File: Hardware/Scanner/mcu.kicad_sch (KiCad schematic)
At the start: 8 parts, among them Q1 BSS138DW-7-F, U6 AS7341-DLGT

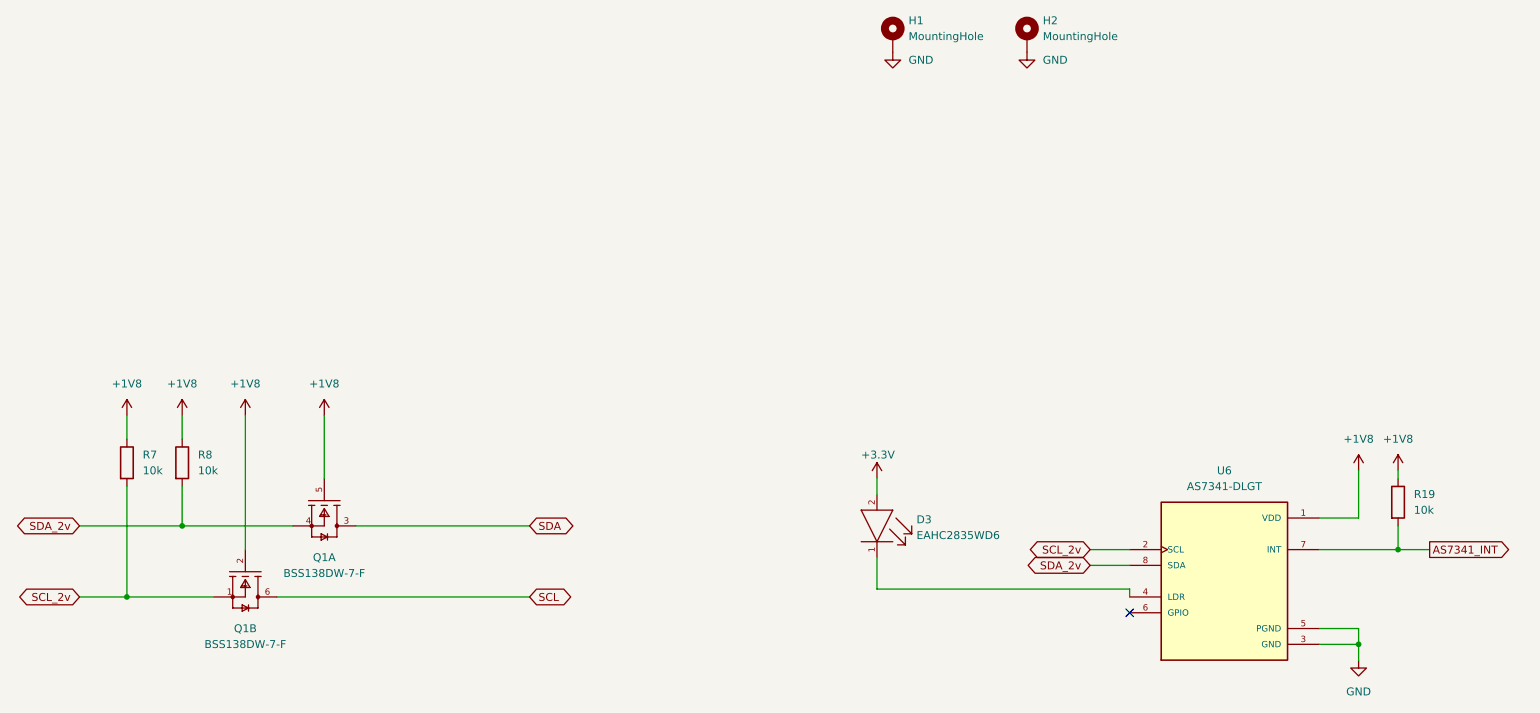
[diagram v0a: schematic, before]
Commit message: added footprint for MTSM2601SMF1-100
Signed-off-by: lokimetasmith <lokimail@gmail.com>
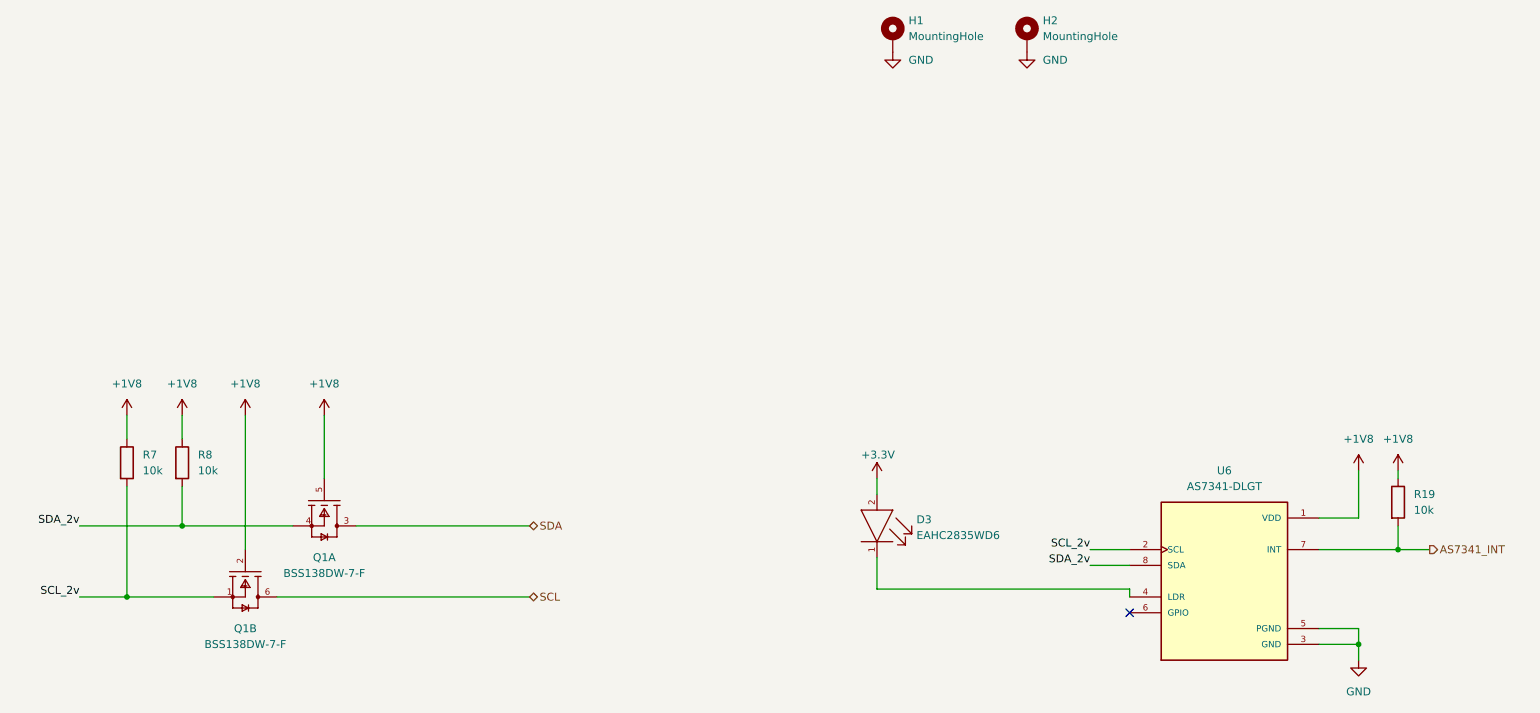
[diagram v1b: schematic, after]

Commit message: lots of changes, added footprints, fixed broken schemaitcs, fixed kicad 7.0 issues
Signed-off-by: lokimetasmith <lokimail@gmail.com>
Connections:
- net +3V3 renamed +3.3V

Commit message: updated schematic, and layout, updated bom, fully converted to 3.3v for Voltage input only
Signed-off-by: lokimetasmith <lokimail@gmail.com>
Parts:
- D3: automotive No -> (none); category Diode -> (none); colour White -> (none); device class L1 Optoelectronics -> (none); device class L2 LEDs -> (none); device class L3 unset -> (none); forward current 150mA -> (none); forward voltage 3.4V -> (none); height 0.85mm -> (none); lead free Yes -> (none); led orientation Top View -> (none); library id 70d3c750636d3268 -> (none); max junction temp +115°C -> (none); package PLCC2 -> (none); power dissipation 630mW -> (none); reverse voltage 5V -> (none); rohs Yes -> (none); temperature range high +85°C -> (none); temperature range low -40°C -> (none); viewing angle 120° -> (none)
- R19, R7, R8: digikey description (none) -> RES 10K OHM 5% 1/10W 0603; digikey part number (none) -> 311-10KGRCT-ND; mouser description (none) -> CRGH0603J10K; mouser part number (none) -> 279-CRGH0603J10K
- U6: digikey description (none) -> SENSOR OPT AMBIENT 8OLGA; digikey part number (none) -> AS7341-DLGTCT-ND
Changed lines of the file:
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@@
+      (effects (font (size 1.27 1.27)) hide)
+    )
+    (property "mouser description" "CRGH0603J10K" (at 68.58 100.33 0)
+      (effects (font (size 1.27 1.27)) hide)
+    )
+    (property "mouser part number" "279-CRGH0603J10K" (at 68.58 100.33 0)
+      (effects (font (size 1.27 1.27)) hide)
+    )
+    (property "digikey description" "RES 10K OHM 5% 1/10W 0603" (at 68.58 100.33 0)
+      (effects (font (size 1.27 1.27)) hide)
+    )
+    (property "digikey part number" "311-10KGRCT-ND" (at 68.58 100.33 0)
       (effects (font (size 1.27 1.27)) hide)
     )
@@
       (effects (font (size 1.27 1.27)) (justify left) hide)
     )
-    (property "automotive" "No" (at 200.66 102.87 0)
-      (effects (font (size 1.27 1.27)) (justify left) hide)
-    )
-    (property "category" "Diode" (at 203.2 102.87 0)
-      (effects (font (size 1.27 1.27)) (justify left) hide)
-    )
-    (property "colour" "White" (at 205.74 102.87 0)
-      (effects (font (size 1.27 1.27)) (justify left) hide)
-    )
-    (property "device class L1" "Optoelectronics" (at 208.28 102.87 0)
-      (effects (font (size 1.27 1.27)) (justify left) hide)
-    )
-    (property "device class L2" "LEDs" (at 210.82 102.87 0)
-      (effects (font (size 1.27 1.27)) (justify left) hide)
-    )
-    (property "device class L3" "unset" (at 213.36 102.87 0)
-      (effects (font (size 1.27 1.27)) (justify left) hide)
-    )
     (property "digikey description" "LED COOL WHITE 6500K 2SMD" (at 215.9 102.87 0)
       (effects (font (size 1.27 1.27)) (justify left) hide)
@@
       (effects (font (size 1.27 1.27)) (justify left) hide)
     )
-    (property "forward current" "150mA" (at 220.98 102.87 0)
-      (effects (font (size 1.27 1.27)) (justify left) hide)
-    )
-    (property "forward voltage" "3.4V" (at 223.52 102.87 0)
-      (effects (font (size 1.27 1.27)) (justify left) hide)
-    )
-    (property "height" "0.85mm" (at 226.06 102.87 0)
-      (effects (font (size 1.27 1.27)) (justify left) hide)
-    )
-    (property "lead free" "Yes" (at 228.6 102.87 0)
-      (effects (font (size 1.27 1.27)) (justify left) hide)
-    )
-    (property "led orientation" "Top View" (at 231.14 102.87 0)
-      (effects (font (size 1.27 1.27)) (justify left) hide)
-    )
-    (property "library id" "70d3c750636d3268" (at 233.68 102.87 0)
-      (effects (font (size 1.27 1.27)) (justify left) hide)
-    )
     (property "manufacturer" "Everlight" (at 236.22 102.87 0)
       (effects (font (size 1.27 1.27)) (justify left) hide)
     )
-    (property "max junction temp" "+115°C" (at 238.76 102.87 0)
-      (effects (font (size 1.27 1.27)) (justify left) hide)
-    )
     (property "mouser description" "White High Power Lighting LED" (at 241.3 102.87 0)
       (effects (font (size 1.27 1.27)) (justify left) hide)
     )
     (property "mouser part number" "638-EAHC2835WD6" (at 243.84 102.87 0)
-      (effects (font (size 1.27 1.27)) (justify left) hide)
-    )
-    (property "package" "PLCC2" (at 246.38 102.87 0)
-      (effects (font (size 1.27 1.27)) (justify left) hide)
-    )
-    (property "power dissipation" "630mW" (at 248.92 102.87 0)
-      (effects (font (size 1.27 1.27)) (justify left) hide)
-    )
-    (property "reverse voltage" "5V" (at 251.46 102.87 0)
-      (effects (font (size 1.27 1.27)) (justify left) hide)
-    )
-    (property "rohs" "Yes" (at 254 102.87 0)
-      (effects (font (size 1.27 1.27)) (justify left) hide)
-    )
-    (property "temperature range high" "+85°C" (at 256.54 102.87 0)
-      (effects (font (size 1.27 1.27)) (justify left) hide)
-    )
-    (property "temperature range low" "-40°C" (at 259.08 102.87 0)
-      (effects (font (size 1.27 1.27)) (justify left) hide)
-    )
-    (property "viewing angle" "120°" (at 261.62 102.87 0)
       (effects (font (size 1.27 1.27)) (justify left) hide)
     )
@@
           (reference "Q1") (unit 1)
         )
+        (path "/a818e058-3544-4da8-96fb-1a428660711f/a8dcb7a4-48cf-403e-b881-d44234291c62"
+          (reference "Q1") (unit 1)
+        )
       )
     )
@@
       (effects (font (size 1.27 1.27)) hide)
     )
+    (property "mouser description" "CRGH0603J10K" (at 264.16 106.68 0)
+      (effects (font (size 1.27 1.27)) hide)
+    )
+    (property "mouser part number" "279-CRGH0603J10K" (at 264.16 106.68 0)
+      (effects (font (size 1.27 1.27)) hide)
+    )
+    (property "digikey description" "RES 10K OHM 5% 1/10W 0603" (at 264.16 106.68 0)
+      (effects (font (size 1.27 1.27)) hide)
+    )
+    (property "digikey part number" "311-10KGRCT-ND" (at 264.16 106.68 0)
+      (effects (font (size 1.27 1.27)) hide)
+    )
     (pin "1")
     (pin "2")
@@
       (effects (font (size 1.27 1.27)) hide)
     )
+    (property "mouser description" "CRGH0603J10K" (at 59.69 100.33 0)
+      (effects (font (size 1.27 1.27)) hide)
+    )
+    (property "mouser part number" "279-CRGH0603J10K" (at 59.69 100.33 0)
+      (effects (font (size 1.27 1.27)) hide)
+    )
+    (property "digikey description" "RES 10K OHM 5% 1/10W 0603" (at 59.69 100.33 0)
+      (effects (font (size 1.27 1.27)) hide)
+    )
+    (property "digikey part number" "311-10KGRCT-ND" (at 59.69 100.33 0)
+      (effects (font (size 1.27 1.27)) hide)
+    )
     (pin "1")
     (pin "2")
@@
       (effects (font (size 1.27 1.27)) (justify left bottom) hide)
     )
-    (pin "1")
+    (property "digikey description" "SENSOR OPT AMBIENT 8OLGA" (at 236.22 119.38 0)
+      (effects (font (size 1.27 1.27)) hide)
+    )
+    (property "digikey part number" "AS7341-DLGTCT-ND" (at 236.22 119.38 0)
+      (effects (font (size 1.27 1.27)) hide)
+    )
+    (pin "1")

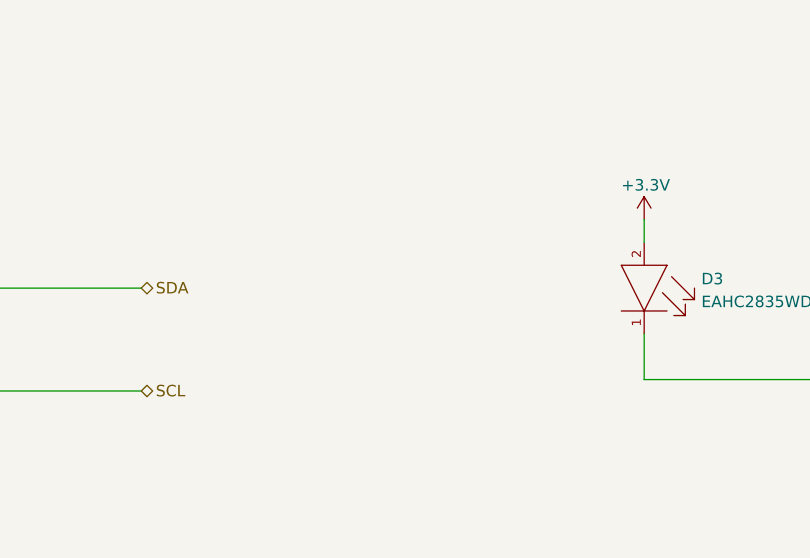
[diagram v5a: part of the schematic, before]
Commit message: added decoupling capactitors, added footprint for 3d model, need to verify new footprint
Signed-off-by: lokimetasmith <lokimail@gmail.com>
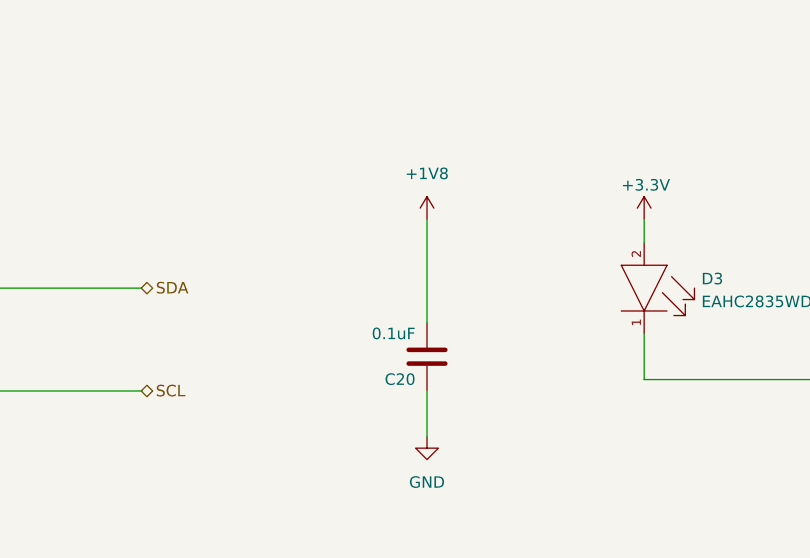
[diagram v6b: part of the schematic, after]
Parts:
- added C20: 0.1uF, Capacitor_SMD:C_0603_1608Metric_Pad1.08x0.95mm_HandSolder, symbol Device:C
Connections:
- net +1V8: now also C20.2
- net GND: now also C20.1
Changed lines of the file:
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@@
+    (stroke (width 0) (type default))
+  )
+  (wire (pts (xy 156.21 102.87) (xy 156.21 114.3))
     (stroke (width 0) (type default))
   )
@@
   )
   (wire (pts (xy 52.07 121.92) (xy 59.69 121.92))
+    (stroke (width 0) (type default))
+  )
+  (wire (pts (xy 156.21 121.92) (xy 156.21 127))
     (stroke (width 0) (type default))
   )
@@
         (path "/a818e058-3544-4da8-96fb-1a428660711f/f3879066-a91b-415e-b241-18f9d05de4a2"
           (reference "#PWR0112") (unit 1)
+        )
+      )
+    )
+  )
+  (symbol (lib_id "power:GND") (at 156.21 127 0) (unit 1)
+    (in_bom yes) (on_board yes) (dnp no) (fields_autoplaced)
+    (property "Reference" "#PWR0125" (at 156.21 133.35 0)
+      (effects (font (size 1.27 1.27)) hide)
+    )
+    (property "Value" "GND" (at 156.21 132.08 0)
+      (effects (font (size 1.27 1.27)))
+    )
+    (property "Footprint" "" (at 156.21 127 0)
+      (effects (font (size 1.27 1.27)) hide)
+    )
+    (property "Datasheet" "" (at 156.21 127 0)
+      (effects (font (size 1.27 1.27)) hide)
+    )
+    (pin "1")
+    (instances
+      (project "RoundScanner"
+        (path "/a818e058-3544-4da8-96fb-1a428660711f/5869e7b3-0d61-455b-97ad-e4e8b4829f27"
+          (reference "#PWR0125") (unit 1)
+        )
+        (path "/a818e058-3544-4da8-96fb-1a428660711f/f3879066-a91b-415e-b241-18f9d05de4a2"
+          (reference "#PWR046") (unit 1)
         )
       )
@@
         (path "/a818e058-3544-4da8-96fb-1a428660711f/f3879066-a91b-415e-b241-18f9d05de4a2"
           (reference "#PWR0109") (unit 1)
+        )
+      )
+    )
+  )
+  (symbol (lib_id "power:+1V8") (at 156.21 102.87 0) (unit 1)
+    (in_bom yes) (on_board yes) (dnp no) (fields_autoplaced)
+    (property "Reference" "#PWR0130" (at 156.21 106.68 0)
+      (effects (font (size 1.27 1.27)) hide)
+    )
+    (property "Value" "+1V8" (at 156.21 97.79 0)
+      (effects (font (size 1.27 1.27)))
+    )
+    (property "Footprint" "" (at 156.21 102.87 0)
+      (effects (font (size 1.27 1.27)) hide)
+    )
+    (property "Datasheet" "" (at 156.21 102.87 0)
+      (effects (font (size 1.27 1.27)) hide)
+    )
+    (pin "1")
+    (instances
+      (project "RoundScanner"
+        (path "/a818e058-3544-4da8-96fb-1a428660711f/5869e7b3-0d61-455b-97ad-e4e8b4829f27"
+          (reference "#PWR0130") (unit 1)
+        )
+        (path "/a818e058-3544-4da8-96fb-1a428660711f/f3879066-a91b-415e-b241-18f9d05de4a2"
+          (reference "#PWR045") (unit 1)
         )
       )
@@
         )
       )
+    )
+  )
+  (symbol (lib_id "Device:C") (at 156.21 118.11 180) (unit 1)
+    (in_bom yes) (on_board yes) (dnp no)
+    (property "Reference" "C20" (at 154.94 120.65 0)
+      (effects (font (size 1.27 1.27)) (justify left))
+    )
+    (property "Value" "0.1uF" (at 154.94 115.57 0)
+      (effects (font (size 1.27 1.27)) (justify left))
+    )
+    (property "Footprint" "Capacitor_SMD:C_0603_1608Metric_Pad1.08x0.95mm_HandSolder" (at 155.2448 114.3 0)
+      (effects (font (size 1.27 1.27)) hide)
+    )
+    (property "Datasheet" "~" (at 156.21 118.11 0)
+      (effects (font (size 1.27 1.27)) hide)
+    )
+    (property "digikey description" "CAP CER 0.1UF 16V X7R 0603" (at 156.21 118.11 0)
+      (effects (font (size 1.27 1.27)) hide)
+    )
+    (property "digikey part number" "311-1088-1-ND" (at 156.21 118.11 0)
+      (effects (font (size 1.27 1.27)) hide)
+    )
+    (pin "1")
+    (pin "2")
+    (instances
+      (project "RoundScanner"
+        (path "/a818e058-3544-4da8-96fb-1a428660711f/5869e7b3-0d61-455b-97ad-e4e8b4829f27"
+          (reference "C20") (unit 1)
+        )
+        (path "/a818e058-3544-4da8-96fb-1a428660711f/f3879066-a91b-415e-b241-18f9d05de4a2"
+          (reference "C20") (unit 1)
+        )
+      )

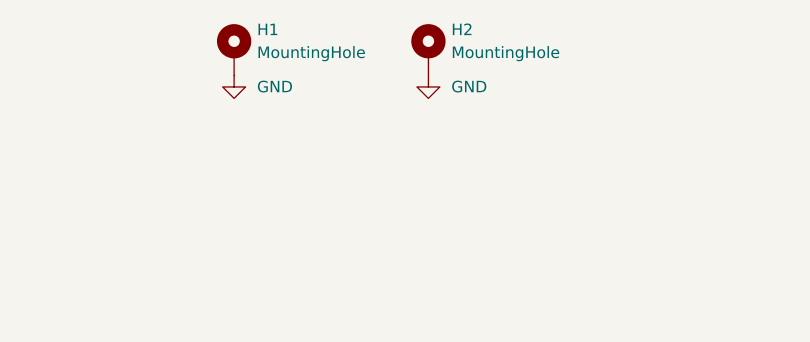
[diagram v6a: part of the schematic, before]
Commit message: cleared all DRC errors
Signed-off-by: lokimetasmith <lokimail@gmail.com>
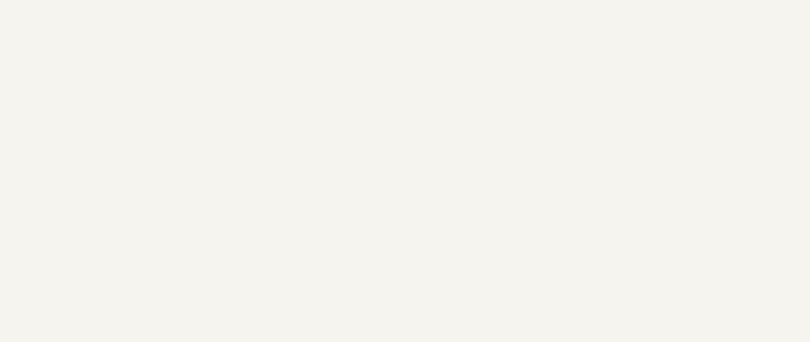
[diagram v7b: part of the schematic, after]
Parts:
- removed H1, H2: MountingHole, MountingHole:MountingHole_2.2mm_M2_ISO7380_Pad, symbol Mechanical:MountingHole_Pad
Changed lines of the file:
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@@
-    )
-  )
-  (symbol (lib_id "power:GND") (at 182.88 34.29 0) (unit 1)
-    (in_bom yes) (on_board yes) (dnp no) (fields_autoplaced)
-    (property "Reference" "#PWR0112" (at 182.88 40.64 0)
-      (effects (font (size 1.27 1.27)) hide)
-    )
-    (property "Value" "GND" (at 185.42 35.5599 0)
-      (effects (font (size 1.27 1.27)) (justify left))
-    )
-    (property "Footprint" "" (at 182.88 34.29 0)
-      (effects (font (size 1.27 1.27)) hide)
-    )
-    (property "Datasheet" "" (at 182.88 34.29 0)
-      (effects (font (size 1.27 1.27)) hide)
-    )
-    (pin "1")
-    (instances
-      (project "RoundScanner"
-        (path "/a818e058-3544-4da8-96fb-1a428660711f/f3879066-a91b-415e-b241-18f9d05de4a2"
-          (reference "#PWR0112") (unit 1)
-        )
-      )
     )
   )
@@
         (path "/a818e058-3544-4da8-96fb-1a428660711f/f3879066-a91b-415e-b241-18f9d05de4a2"
           (reference "#PWR046") (unit 1)
-        )
-      )
-    )
-  )
-  (symbol (lib_id "Mechanical:MountingHole_Pad") (at 204.47 31.75 0) (unit 1)
-    (in_bom no) (on_board yes) (dnp no) (fields_autoplaced)
-    (property "Reference" "H2" (at 207.01 29.2099 0)
-      (effects (font (size 1.27 1.27)) (justify left))
-    )
-    (property "Value" "MountingHole" (at 207.01 31.7499 0)
-      (effects (font (size 1.27 1.27)) (justify left))
-    )
-    (property "Footprint" "MountingHole:MountingHole_2.2mm_M2_ISO7380_Pad" (at 204.47 31.75 0)
-      (effects (font (size 1.27 1.27)) hide)
-    )
-    (property "Datasheet" "~" (at 204.47 31.75 0)
-      (effects (font (size 1.27 1.27)) hide)
-    )
-    (pin "1")
-    (instances
-      (project "RoundScanner"
-        (path "/a818e058-3544-4da8-96fb-1a428660711f/f3879066-a91b-415e-b241-18f9d05de4a2"
-          (reference "H2") (unit 1)
         )
       )
@@
     )
   )
-  (symbol (lib_id "Mechanical:MountingHole_Pad") (at 182.88 31.75 0) (unit 1)
-    (in_bom no) (on_board yes) (dnp no) (fields_autoplaced)
-    (property "Reference" "H1" (at 185.42 29.2099 0)
-      (effects (font (size 1.27 1.27)) (justify left))
-    )
-    (property "Value" "MountingHole" (at 185.42 31.7499 0)
-      (effects (font (size 1.27 1.27)) (justify left))
-    )
-    (property "Footprint" "MountingHole:MountingHole_2.2mm_M2_ISO7380_Pad" (at 182.88 31.75 0)
-      (effects (font (size 1.27 1.27)) hide)
-    )
-    (property "Datasheet" "~" (at 182.88 31.75 0)
-      (effects (font (size 1.27 1.27)) hide)
-    )
-    (pin "1")
-    (instances
-      (project "RoundScanner"
-        (path "/a818e058-3544-4da8-96fb-1a428660711f/f3879066-a91b-415e-b241-18f9d05de4a2"
-          (reference "H1") (unit 1)
-        )
-      )
-    )
-  )
   (symbol (lib_id "power:+1V8") (at 264.16 101.6 0) (unit 1)
     (in_bom yes) (on_board yes) (dnp no) (fields_autoplaced)
@@
         )
       )
-    )
-  )
-  (symbol (lib_id "power:GND") (at 204.47 34.29 0) (unit 1)
-    (in_bom yes) (on_board yes) (dnp no) (fields_autoplaced)
-    (property "Reference" "#PWR0108" (at 204.47 40.64 0)
-      (effects (font (size 1.27 1.27)) hide)
-    )
-    (property "Value" "GND" (at 207.01 35.5599 0)
-      (effects (font (size 1.27 1.27)) (justify left))
-    )
-    (property "Footprint" "" (at 204.47 34.29 0)
-      (effects (font (size 1.27 1.27)) hide)
-    )
-    (property "Datasheet" "" (at 204.47 34.29 0)
-      (effects (font (size 1.27 1.27)) hide)
-    )
-    (pin "1")
-    (instances
-      (project "RoundScanner"
-        (path "/a818e058-3544-4da8-96fb-1a428660711f/f3879066-a91b-415e-b241-18f9d05de4a2"
-          (reference "#PWR0108") (unit 1)
-        )
-      )
